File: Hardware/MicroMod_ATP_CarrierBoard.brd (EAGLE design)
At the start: 83.8 x 55.9 mm, 66 parts, among them J19 QWIIC_RIGHT_ANGLE, J2 JTAG, J20 QWIIC_RIGHT_ANGLE, J21 1X04_SMD_STRAIGHT_COMBO, J23 1X04_SMD_STRAIGHT_COMBO, J4 USB_A_SMT_FEMALE, J6 MICROMOD-2222-C, J8 1X04_SMD_STRAIGHT_COMBO, U5 AP7361C-33

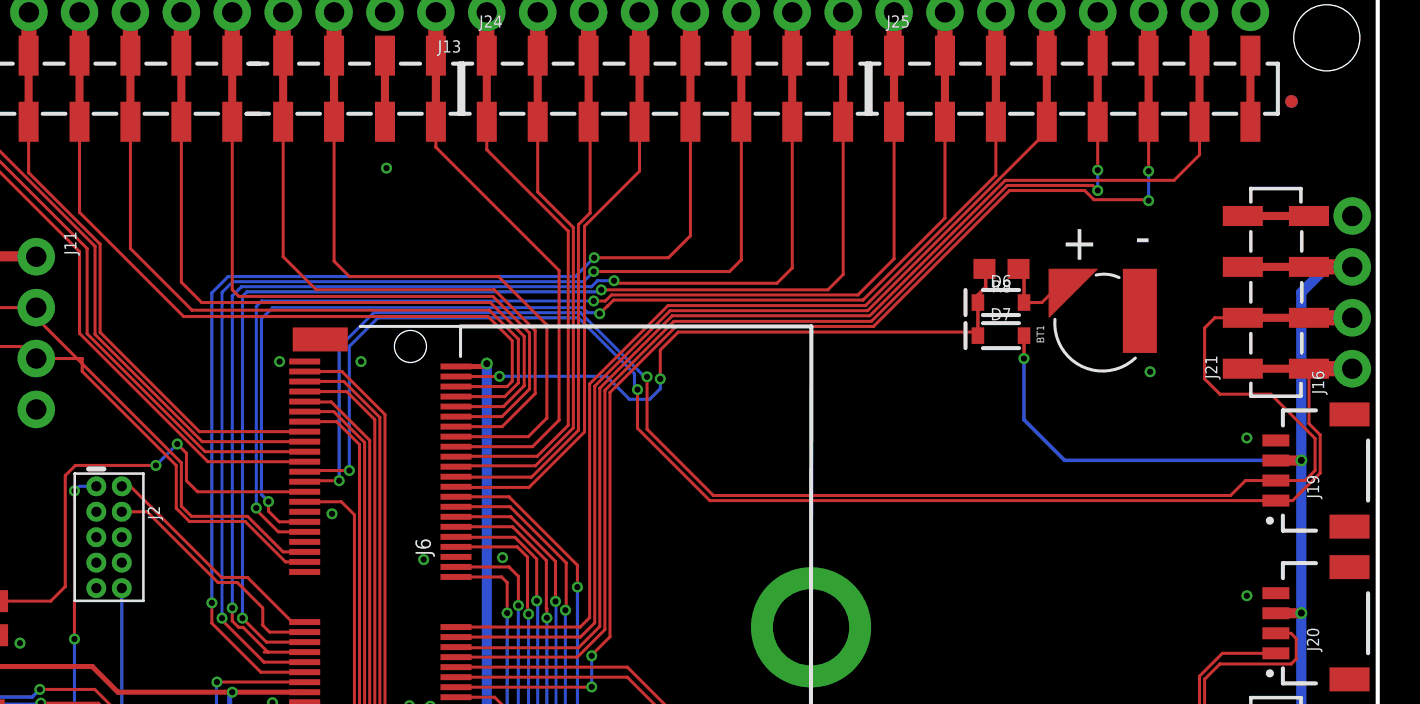
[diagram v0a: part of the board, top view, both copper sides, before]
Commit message: Moves a few traces - again for 90 degree intersections
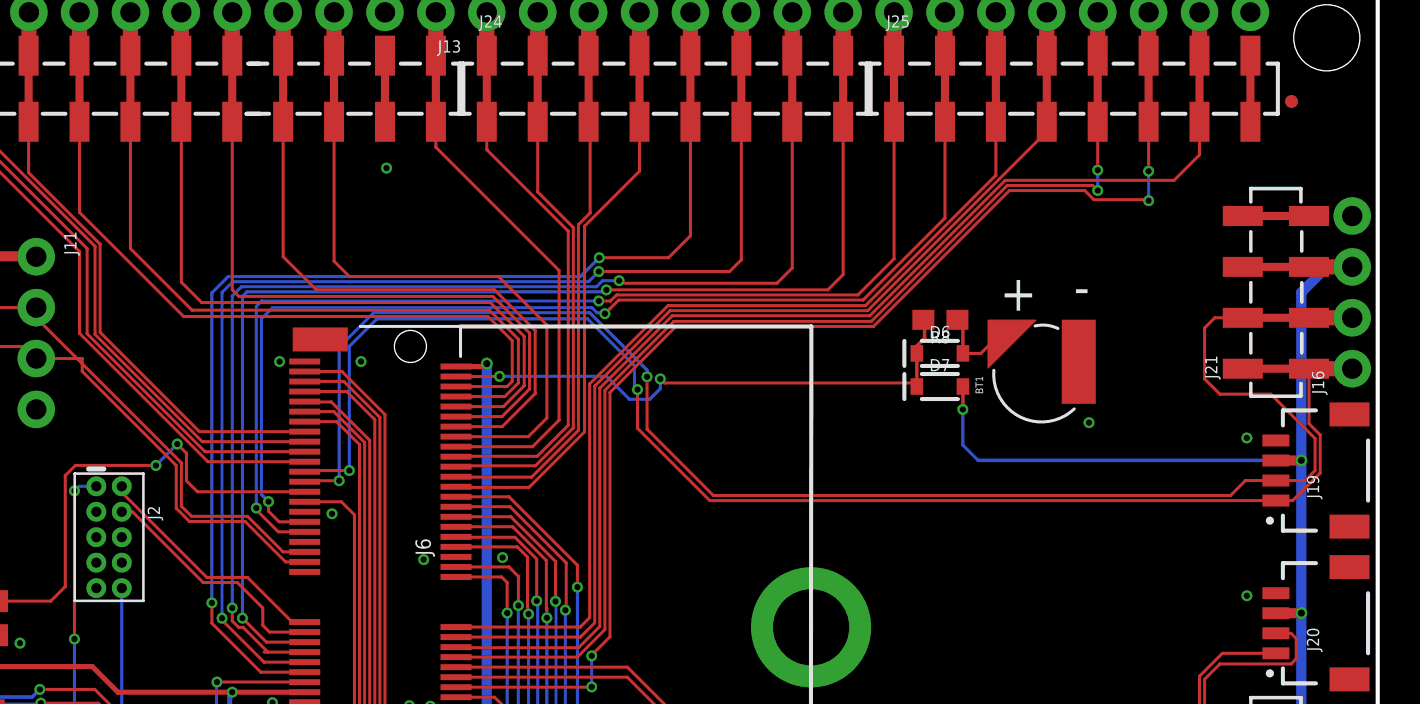
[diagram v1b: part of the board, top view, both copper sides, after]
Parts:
- moved R8 3.97 mm to (62.0, 39.3)
- moved BT1 3.97 mm to (67.1, 36.6)
- moved D6 3.97 mm to (62.0, 37.6)
- moved D7 3.97 mm to (62.0, 35.9)
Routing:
- net RTC_3V: track 32.6 -> 27.8 mm
- net 3.3V: track 196.4 -> 197.7 mm

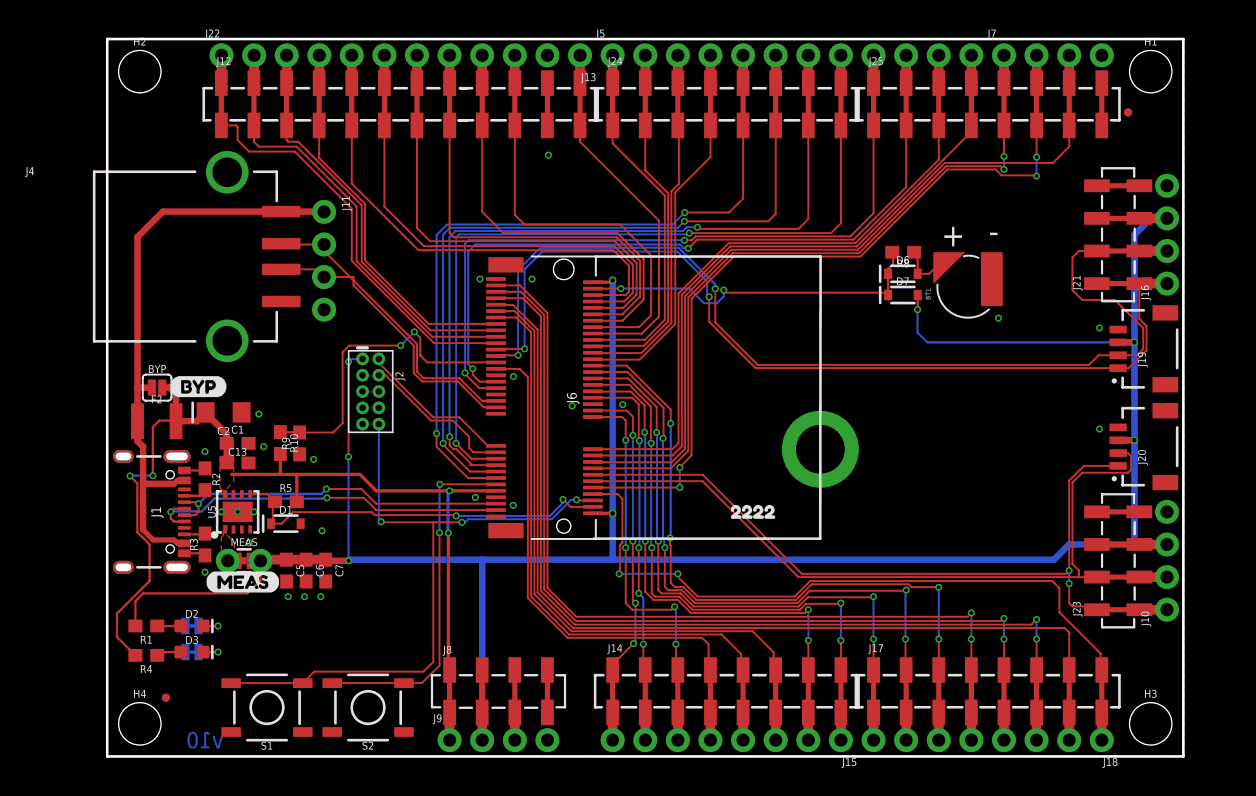
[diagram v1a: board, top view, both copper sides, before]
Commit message: Shifts top header assignements to the left to make space for 3v3 and GND pins
* Adds top silk to almost all pins
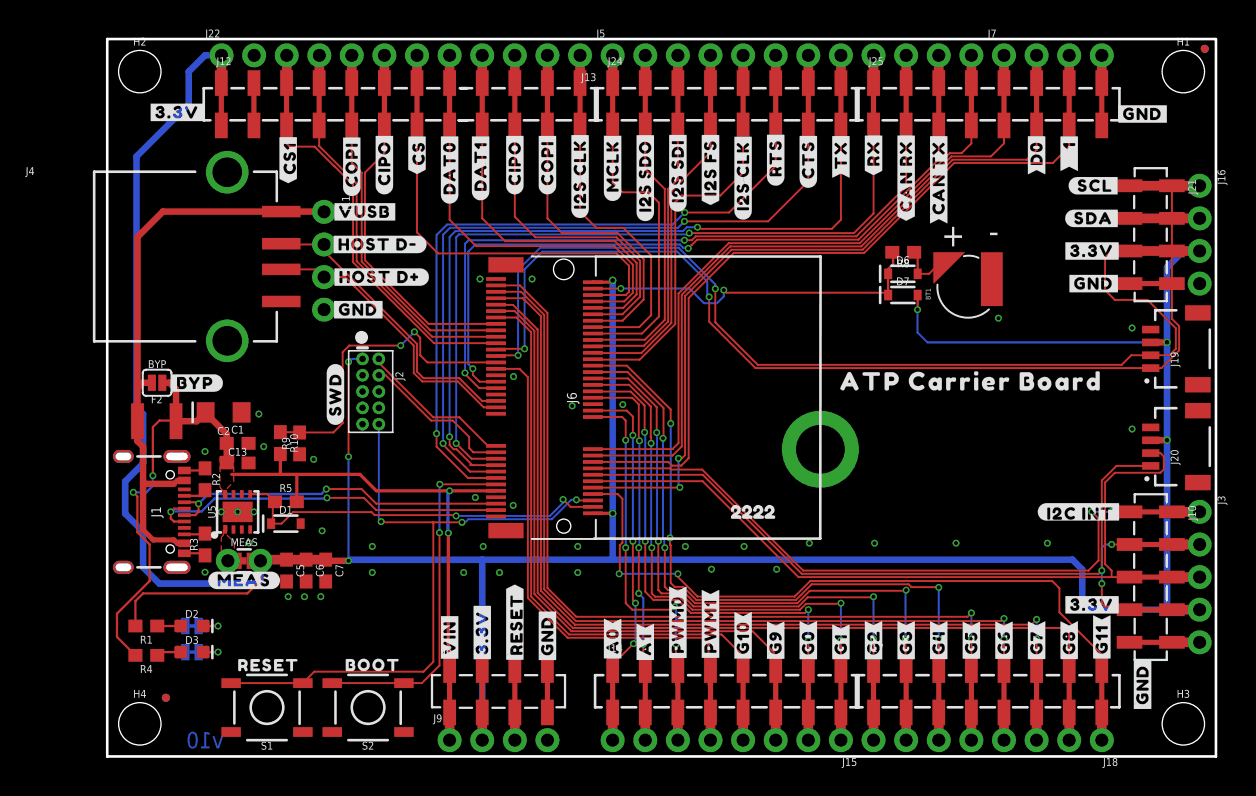
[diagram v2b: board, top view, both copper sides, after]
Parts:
- removed J23: 1X04_SMD_STRAIGHT_COMBO, SparkFun-Connectors:1X04_SMD_VERTICAL_COMBO
- added J3: (no value), SparkFun-Connectors:1X05_NO_SILK
- added U$1: (no value), ana:#A0#10
- added U$10: (no value), ana:#G4#4
- added U$11: (no value), ana:#G5#5
- added U$12: (no value), ana:#G6#6
- added U$13: (no value), ana:#G7#7
- added U$14: (no value), ana:#G8#8
- added U$15: (no value), ana:#G9#9
- added U$16: (no value), ana:#G10#10
- added U$17: (no value), ana:#G11#10
- added U$18: (no value), ana:#PWM0#10
- added U$19: (no value), ana:#PWM1#10
- added U$2: (no value), ana:#A1#10
- added U$20: (no value), headtop:##CS#1
- added U$21: (no value), headtop:##I2C_INT#10
- added U$22: (no value), headtop:#CAN_RX#9
- added U$23: (no value), headtop:#CAN_TX#10
- added U$24, U$56: (no value), headtop:#CIPO#3
- added U$25, U$57: (no value), headtop:#COPI#2
- added U$26: (no value), headtop:#CTS#6
- added U$28, U$52: (no value), headtop:#I2S_CLK#5
- added U$29: (no value), headtop:#I2S_FS#5
- added U$3: (no value), ana:#D1#1
- added U$30: (no value), headtop:#I2S_SDI#5
- added U$31: (no value), headtop:#I2S_SDO#5
- added U$32: (no value), headtop:#MCLK#4
- added U$33: (no value), headtop:#RTS#5
- added U$34: (no value), headtop:#RX#8
- added U$35: (no value), headtop:#TX#7
- added U$36: (no value), headtop:ATP_CARRIER_BOARD0
- added U$37: (no value), power:##RESET#7
- added U$38, U$60, U$61, U$62: (no value), power:#3#3V#1
- added U$39: (no value), power:#BYP#8
- added U$4: (no value), ana:#G0#2
- added U$40: (no value), power:#HOST_D##9
- added U$41: (no value), power:#HOST_D##10
- added U$42: (no value), power:#MEAS#10
- added U$43: (no value), power:BOOT10
- added U$44: (no value), power:#SDA#4
- added U$45: (no value), power:#VIN#6
- added U$46, U$47, U$48, U$58: (no value), power:#GND#0
- added U$49: (no value), power:#SCL#5
- added U$50: (no value), power:#VUSB#10
- added U$51: (no value), power:#SWD#10
- added U$53: (no value), headtop:#DAT1#4
- added U$54: (no value), headtop:#DAT0#4
- added U$59: (no value), headers_dup:##CS1#0
- added U$6: (no value), ana:#D0#0
- added U$7: (no value), ana:#G1#2
- added U$8: (no value), ana:#G2#2
- added U$9: (no value), ana:#G3#3
- J10: device SparkFun-Connectors:1X04_NO_SILK -> SparkFun-Connectors:1X05_SMD_VERTICAL_COMBO
- U$27: device SparkFun-Buzzard:BYP -> power:#GND#0
- U$5: device SparkFun-Buzzard:MEAS -> power:#RESET10
- moved U$27 35.3 mm to (34.3, 9.40), turned to 90 degrees
- moved U$5 8.05 mm to (12.6, 7.24)
- moved J16 8.03 mm to (85.1, 44.5), turned to 270 degrees
- moved J21 8.03 mm to (81.3, 44.5), turned to 270 degrees
- moved FD2 7.76 mm to (85.5, 55.1)
- moved FD4 7.76 mm to (85.5, 55.1)
- moved J10 7.73 mm to (81.3, 19.1), turned to 270 degrees
- moved J19 2.54 mm to (81.3, 31.8)
- moved J20 2.54 mm to (81.3, 24.1)
- moved H1 2.54 mm to (83.8, 53.3)
- moved H3 2.54 mm to (83.8, 2.54)
- moved BYP 0.38 mm to (3.89, 29.1)
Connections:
- removed net !CS!: J12.5, J12.5@2, J13.8, J6.70
- removed net MISO1: J12.4, J12.4@2, J22.4, J6.61
- removed net MOSI1: J12.3, J12.3@2, J22.3, J6.59
- removed net SCLK1: J12.2, J12.2@2, J22.2, J6.57
- removed net SD_DAT1: J12.7, J12.7@2, J13.6, J6.66
- removed net SD_DAT2: J12.6, J12.6@2, J13.7, J6.68
- removed net SPI_MISO: J12.8, J12.8@2, J13.5, J6.64
- removed net SPI_MOSI: J12.9, J12.9@2, J13.4, J6.62
- removed net SPI_SCK: J12.10, J12.10@2, J13.3, J6.60
- new net !CS!/DAT3: J12.7, J12.7@2, J13.6, J6.70
- new net CIPO/DAT0: J12.10, J12.10@2, J13.3, J6.64
- new net CIPO1: J12.6, J12.6@2, J13.7, J6.61
- new net COPI: J12.11, J12.11@2, J13.2, J6.62
- new net COPI1: J12.5, J12.5@2, J13.8, J6.59
- new net DAT1: J12.9, J12.9@2, J13.4, J6.66
- new net DAT2: J12.8, J12.8@2, J13.5, J6.68
- new net SCK: J12.12, J12.12@2, J13.1, J6.60
- new net SCK1: J12.4, J12.4@2, J22.4, J6.57
- net !CS1: now also J12.3, J12.3@2, J22.3; no longer J12.1, J12.1@2, J22.1
- net 3.3V: now also J10.4, J10.4-2, J12.1, J12.1@2, J22.1, J3.4; no longer J10.3, J23.3, J23.3-2
- net CAN_RXI: now also J25.2, J25.2@2, J5.10; no longer J25.1, J25.1@2, J5.9
- net CAN_TXO: now also J25.3, J25.3@2, J5.11; no longer J25.2, J25.2@2, J5.10
- net CTS1: now also J24.7, J24.7@2, J5.7; no longer J24.6, J24.6@2, J5.6
- net GND: now also J10.5, J10.5-2, J12.2, J12.2@2, J22.2, J3.5; no longer J10.4, J12.11, J12.11@2, J13.2, J23.4, J23.4-2
- net I2C_!INT: now also J10.1, J10.1-2, J3.1; no longer J25.5, J25.5@2, J7.1
- net I2S_CLK: now also J24.5, J24.5@2, J5.5; no longer J24.4, J24.4@2, J5.4
- net I2S_SDI: now also J24.3, J24.3@2, J5.3; no longer J24.2, J24.2@2, J5.2
- net I2S_SDO: now also J24.2, J24.2@2, J5.2; no longer J24.1, J24.1@2, J5.1
- net I2S_WS: now also J24.4, J24.4@2, J5.4; no longer J24.3, J24.3@2, J5.3
- net MCLK: now also J24.1, J24.1@2, J5.1; no longer J12.12, J12.12@2, J13.1
- net RTS1: now also J24.6, J24.6@2, J5.6; no longer J24.5, J24.5@2, J5.5
- net RX1: now also J25.1, J25.1@2, J5.9; no longer J24.8, J24.8@2, J5.8
- net RX2: now also J25.5, J25.5@2, J7.1; no longer J25.4, J25.4@2, J5.12
- net SCL: now also J10.2, J10.2-2, J3.2; no longer J10.1, J23.1, J23.1-2
- net SDA: now also J10.3, J10.3-2, J3.3; no longer J10.2, J23.2, J23.2-2
- net TX1: now also J24.8, J24.8@2, J5.8; no longer J24.7, J24.7@2, J5.7
- net TX2: now also J25.4, J25.4@2, J5.12; no longer J25.3, J25.3@2, J5.11
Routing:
- net 3.3V: track 197.7 -> 269.0 mm
- net SD_DAT2: track 35.0 -> 0.00 mm
- net !CS!: track 34.7 -> 0.00 mm
- net SD_DAT1: track 34.4 -> 0.00 mm
- net SPI_MISO: track 33.0 -> 0.00 mm
- net !CS!/DAT3: track 0.00 -> 32.7 mm
- net SCLK1: track 30.8 -> 0.00 mm
- net DAT2: track 0.00 -> 30.5 mm
- net SPI_MOSI: track 30.5 -> 0.00 mm
- net SPI_SCK: track 30.3 -> 0.00 mm
- net DAT1: track 0.00 -> 28.9 mm
- net MOSI1: track 28.0 -> 0.00 mm
- net CIPO/DAT0: track 0.00 -> 27.2 mm
- net SCK1: track 0.00 -> 26.9 mm
- net MISO1: track 26.1 -> 0.00 mm
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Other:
- board size 83.8 x 55.9 mm -> 86.4 x 55.9 mm

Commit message: Adds the rest of the header labels, fixes or approves DRC errors
* adds Qwiic Mount screw holes
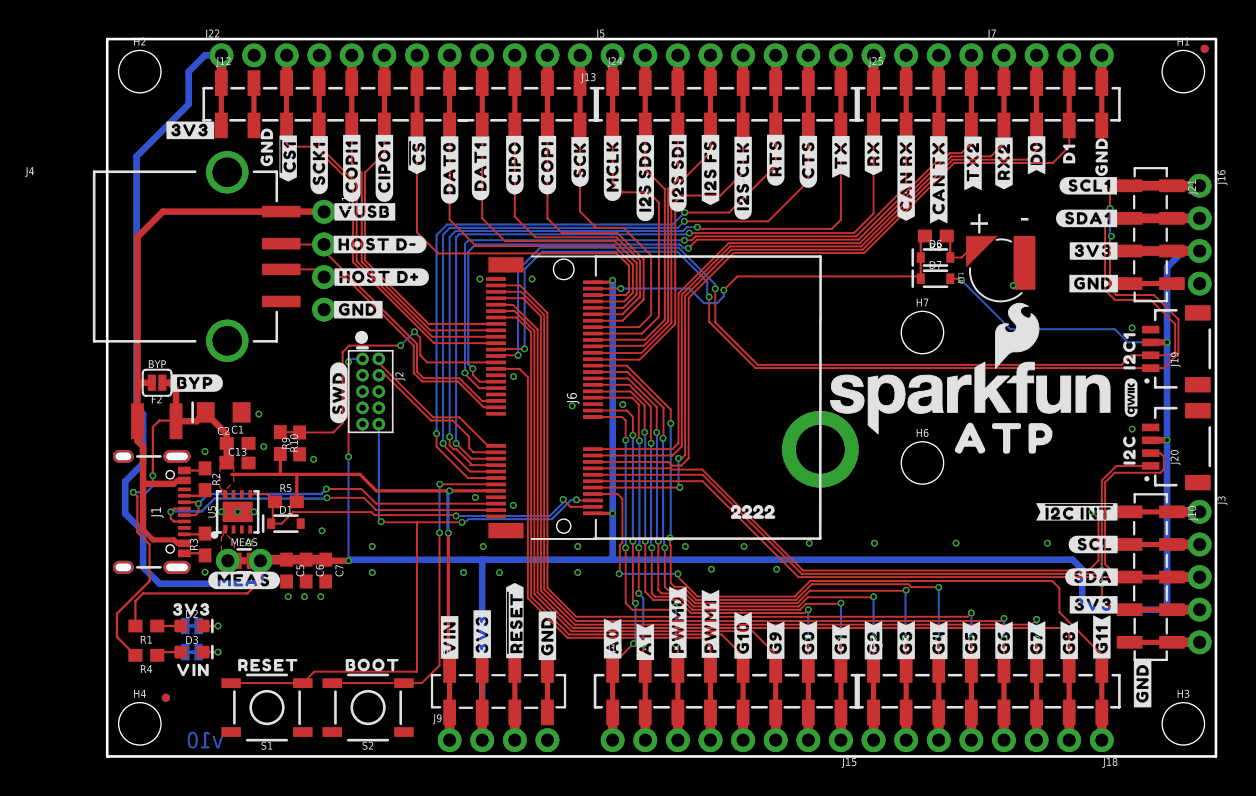
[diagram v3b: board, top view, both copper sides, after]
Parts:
- added H6, H7: STAND-OFF, SparkFun-Hardware:STAND-OFF
- added LOGO1, LOGO4: SFE_LOGO_NAME_FLAME.2_INCH, SparkFun-Aesthetics:SFE_LOGO_NAME_FLAME_.2
- added LOGO2: QWIIC_LOGO_3MM, SparkFun-Aesthetics:QWIIC_3MM
- added U$100, U$101, U$102, U$103, U$104, U$105: (no value), fl3:#GND#0
- added U$106, U$107, U$126, U$88: (no value), fl3:#3V3#1
- added U$108: (no value), fl3:#SDA#4
- added U$109: (no value), fl3:#SCL#5
- added U$110: (no value), fl2:##I2C_INT##10
- added U$111: (no value), fl4:#G11#10
- added U$112: (no value), fl4:#G8#8
- added U$113: (no value), fl4:#G7#7
- added U$114: (no value), fl4:#G6#6
- added U$115: (no value), fl4:#G5#5
- added U$116: (no value), fl4:#G4#4
- added U$117: (no value), fl4:#G3#3
- added U$118: (no value), fl4:#G2#2
- added U$119: (no value), fl4:#G1#2
- added U$120: (no value), fl4:#G0#2
- added U$121: (no value), fl4:#PWM0#10
- added U$122: (no value), fl4:#PWM1#10
- added U$123: (no value), fl4:#A0#10
- added U$124: (no value), fl4:#A1#10
- added U$125: (no value), fl3:##RESET##7
- added U$127: (no value), fl3:#VIN#6
- added U$128: (no value), fl3:#HOST_D##9
- added U$129: (no value), fl3:#HOST_D##10
- added U$130: (no value), fl3:#VUSB#10
- added U$131: (no value), fl3:#SWD#10
- added U$132: (no value), fl3:#MEAS#10
- added U$133: (no value), fl3:#VIN_LED#10
- added U$134: (no value), fl3:#3V3_LED#10
- added U$135: (no value), fl4:#G9#ADC##CAM_HSYNC#9
- added U$136: (no value), fl4:#G10#ADC##CAM_VSYNC#10
- added U$137: (no value), fl2:#I2S_SDI#CAM_PCLK#7
- added U$138: (no value), fl2:#I2S_SDO#CAM_MCLK#7
- added U$139: (no value), ana:D11
- added U$63: (no value), headers_dup:#RX2#3
- added U$64: (no value), headers_dup:#TX2#2
- added U$65: (no value), headers_dup:#SCL1#3
- added U$66: (no value), headers_dup:#SDA1#3
- added U$67: (no value), headers_dup:#SCK1#2
- added U$68: (no value), headers_dup:VIN3
- added U$69: (no value), headers_dup:3V34
- added U$70: (no value), power:#3V3#1
- added U$71: (no value), headers_dup:I2C4
- added U$72: (no value), headers_dup:I2C14
- added U$73: (no value), headers_dup:ATP_CARRIER_BOARD1
- added U$74: (no value), fl1:#CIPO1#2
- added U$75: (no value), fl1:#COPI1#2
- added U$76: (no value), fl1:#RX2#3
- added U$77: (no value), fl1:#SCK1#2
- added U$78: (no value), fl1:#SCL1#3
- added U$79: (no value), fl1:#SDA1#3
- added U$80: (no value), fl1:#TX2#2
- added U$81: (no value), fl2:##CS##DAT3#0
- added U$82: (no value), fl2:#DAT2#5
- added U$83: (no value), fl2:#DAT1#5
- added U$84: (no value), fl2:#CIPO#DAT0#5
- added U$85: (no value), fl2:#COPI#4
- added U$86: (no value), fl2:#SCK#4
- added U$87: (no value), fl2:#MCLK#6
- added U$89: (no value), headers_dup:GND4
- added U$90: (no value), fl2:#I2S_FS#7
- added U$91: (no value), fl2:#I2S_CLK#7
- added U$92: (no value), fl2:#RTS#7
- added U$93: (no value), fl2:#CTS#8
- added U$94: (no value), fl2:#TX#9
- added U$95: (no value), fl2:#RX#10
- added U$96: (no value), fl2:#CAN_RX#10
- added U$97: (no value), fl2:#CAN_TX#10
- added U$98: (no value), fl4:#D0#0
- U$20: device headtop:##CS#1 -> headers_dup:##CS1##2
- U$21: device headtop:##I2C_INT#10 -> headtop:##I2C_INT##10
- U$28: device headtop:#I2S_CLK#5 -> headtop:#SCK#2
- U$3: device ana:#D1#1 -> headers_dup:GND4
- U$36: device headtop:ATP_CARRIER_BOARD0 -> fl1:##CS1##0
- U$37: device power:##RESET#7 -> power:##RESET##7
- U$38, U$60, U$61: device power:#3#3V#1 -> power:#3V3#1
- U$48: device power:#GND#0 -> fl4:D11
- U$56: device headtop:#CIPO#3 -> headers_dup:#CIPO1#2
- U$57: device headtop:#COPI#2 -> headers_dup:#COPI1#2
- U$59: device headers_dup:##CS1#0 -> headtop:##CS##0
- U$62: device power:#3#3V#1 -> headers_dup:ATP0
- moved U$61 79.4 mm to (6.48, 48.8)
- moved U$62 69.3 mm to (70.0, 24.8)
- moved U$36 58.1 mm to (14.0, 52.2), flipped to the bottom, turned to 270 degrees
- moved U$49 27.9 mm to (77.0, 16.5)
- moved U$44 27.9 mm to (76.8, 14.0)
- moved U$59 10.0 mm to (24.1, 47.0)
- moved U$20 10.0 mm to (14.1, 46.7)
- moved U$48 6.31 mm to (74.9, 52.7), flipped to the bottom, turned to 270 degrees
- moved D6 2.84 mm to (64.5, 38.9)
- moved BT1 2.84 mm to (69.6, 37.8)
- moved D7 2.84 mm to (64.5, 37.2)
- moved R8 2.84 mm to (64.5, 40.5)
- moved U$3 2.57 mm to (77.5, 46.7)
- moved U$28 1.14 mm to (36.8, 46.5)
- moved U$51 0.28 mm to (18.0, 28.3)
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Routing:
- net SCL1: track 84.6 -> 89.8 mm, vias 2 -> 4
- net 3.3V: track 269.0 -> 265.3 mm
- net SDA1: track 84.8 -> 87.7 mm
- net RTC_3V: track 27.8 -> 30.7 mm
- net PWM1: track 40.5 -> 39.4 mm
- net PWM0: track 29.0 -> 27.9 mm
- net !RESET: track 52.3 -> 51.4 mm
